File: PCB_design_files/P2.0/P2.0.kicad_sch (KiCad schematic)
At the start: 28 parts, among them J1 EEG+, J2 EEG-, U1 INA819IDRGR, U2 TLV9102

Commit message: More P2.0 schematic work
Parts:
- added BT1: BHSD-1225-SM, BHSD-1225-SM:BAT_BHSD-1225-SM, symbol Device:Battery_Cell
- added C10, C11: 10uF, Capacitor_SMD:C_0805_2012Metric, symbol Device:C
- added C8: 2.2uF, Capacitor_SMD:C_0402_1005Metric, symbol Device:C
- added C9: 33uF, Capacitor_SMD:C_0805_2012Metric, symbol Device:C
- added D1: LED, symbol Device:LED
- added L1: 2.2uH, symbol Device:L
- added R18, R19: 1.1k, Resistor_SMD:R_0402_1005Metric, symbol Device:R
- added U3: TPS61094, symbol My_Library:TPS61094
- added U4: TC1044S, symbol Regulator_SwitchedCapacitor:LTC1044
- added U5: NRF52832-QFAA-R, QFN-48_NOR, symbol NRF52832_QFAA:NRF52832-QFAA-R
- C1, C2, C7: footprint Library:CL10A106MQ8NNNC -> Capacitor_SMD:C_0805_2012Metric
- C3, C4, C5, C6: footprint Library:CL10A106MQ8NNNC -> Capacitor_SMD:C_0201_0603Metric
- R10, R11, R12, R13, R14, R2, R3, R4, R5, R6, R7, R8, R9: footprint (none) -> Resistor_SMD:R_0402_1005Metric
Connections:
- net +3V3: now also C9.2, U3.10 (VOUT), U4.8 (V+)
- net -3V3: now also C11.2, U4.5 (VOUT)
- net GND: now also BT1.2 (-), C11.1, C8.1, C9.1, D1.1 (K), R19.2, U3.11 (ICHG), U3.12 (VCHG), U3.7 (PGND), U3.8 (AGND), U4.3 (GND), U4.6 (LV)
- new net: C10.1, U4.4 (CAP-)
- new net: C10.2, U4.2 (CAP+)
- new net: BT1.1 (+), C8.2, L1.1, R18.1, U3.2 (MODE), U3.3 (EN), U3.4 (VIN), U3.6 (SUP)
- new net: L1.2, U3.5 (SW)
- new net: R19.1, U3.1 (OSEL)
- new net: D1.2 (A), R18.2
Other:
- note added: "2.Power Supply"
- note added: "3.Microcontroller"
- company: (none) -> JY-68
- title: (none) -> Wearable EEG Sensor
- moved on the sheet: C1, C2, C3, C4, C5, C6, C7, J1, J2, R1, R10, R11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

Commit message: Started PCB
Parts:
- L1: footprint (none) -> Inductor_SMD:L_Murata_DFE201610P
- R16, R17: footprint (none) -> Resistor_SMD:R_0402_1005Metric
- R18: footprint Resistor_SMD:R_0402_1005Metric -> (none)
- U5: footprint QFN-48_NOR -> (none)
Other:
- moved on the sheet: BT1, C10, C11, C8, C9, D1, L1, R18, R19, U3, U4, U5

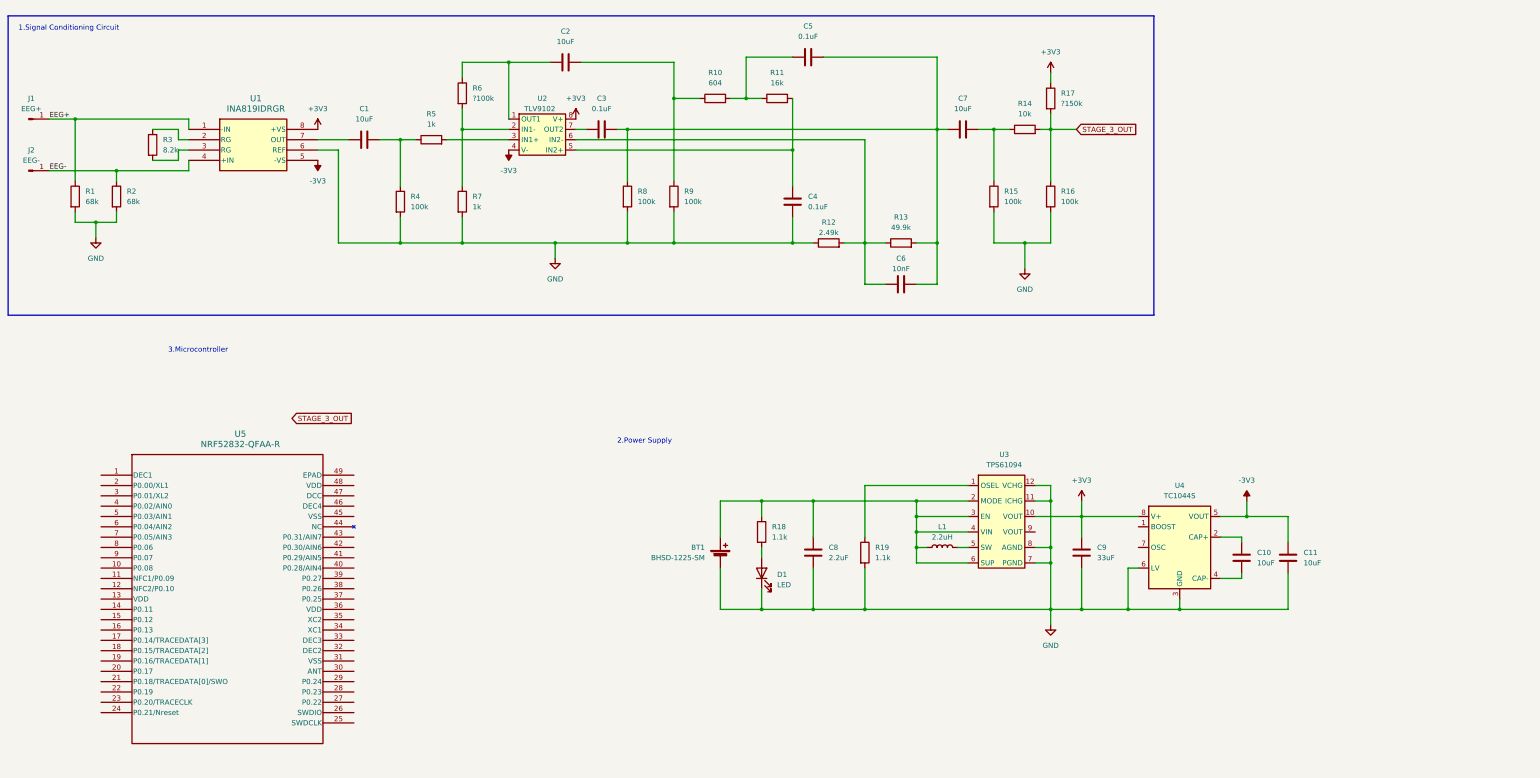
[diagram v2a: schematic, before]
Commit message: PCB layout and component footprint updates
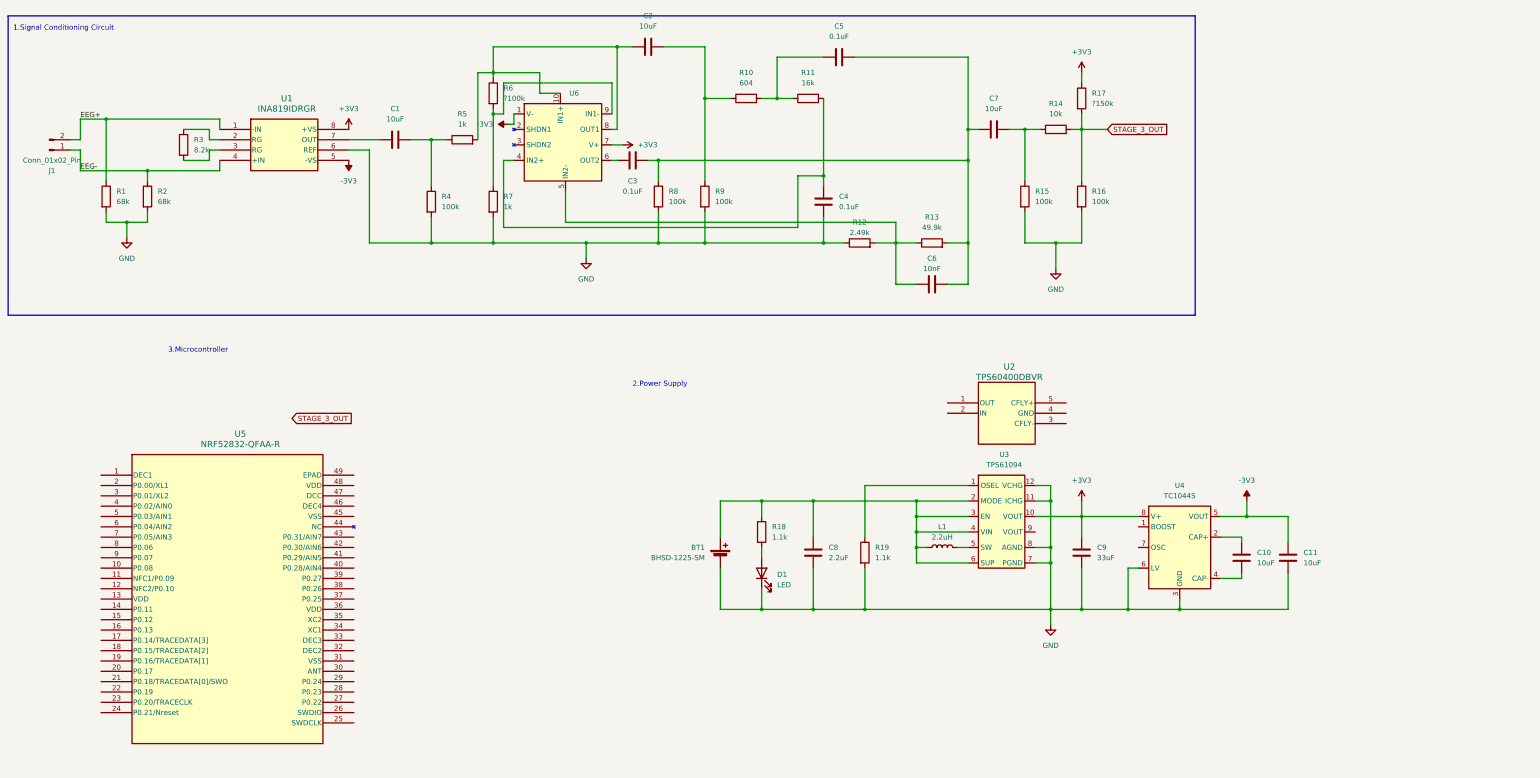
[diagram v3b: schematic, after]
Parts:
- removed J1: EEG+, symbol Connector:Conn_01x01_Pin
- removed J2: EEG-, symbol Connector:Conn_01x01_Pin
- removed U2: TLV9102, symbol My_Library:TLV9102
- added J1: Conn_01x02_Pin, Connector_JST:JST_SH_BM02B-SRSS-TB_1x02-1MP_P1.00mm_Vertical, symbol Connector:Conn_01x02_Pin
- added U2: TPS60400DBVR, DBV5, symbol TPS60400DBVR:TPS60400DBVR
- added U6: ~, symbol TLV9102SIRUGR:TLV9102
- BT1: footprint BHSD-1225-SM:BAT_BHSD-1225-SM -> Connector_JST:JST_ACH_BM02B-ACHSS-GAN-ETF_1x02-1MP_P1.20mm_Vertical
- D1: footprint (none) -> LED_SMD:LED_0402_1005Metric
- R15, R18: footprint (none) -> Resistor_SMD:R_0402_1005Metric
- U3: footprint (none) -> Library:TPS61094DSSR
- U4: footprint (none) -> Library:TC1044SEOA713
- U5: footprint (none) -> Library:QFN-48_NOR
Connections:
- net +3V3: now also U6.7 (V+)
- net -3V3: now also U6.1 (V-)
- net EEG+: now also J1.2 (Pin_2)
- net EEG-: now also J1.1 (Pin_1)
- net at C6.1, R12.2, R13.1: now also U6.5 (IN2-)
- net at C2.1, R6.1: now also R5.2, U6.10 (IN1+), U6.8 (OUT1)
- net at R6.2, R7.1: now also U6.9 (IN1-)
- net at C4.2, R11.2: now also U6.4 (IN2+)
- net at C3.1: now also U6.6 (OUT2)
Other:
- moved on the sheet: C1, C2, C3, C4, C5, C6, C7, R1, R10, R11, R12, R13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

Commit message: Done
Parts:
- removed U4: TC1044S, Library:TC1044SEOA713, symbol Regulator_SwitchedCapacitor:LTC1044
- C10, C11: value 10uF -> 1uF
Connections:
- net +3V3: now also U2.2 (IN)
- net -3V3: now also U2.1 (OUT)
- net GND: now also U2.4 (GND)
- net at C10.1: now also U2.5 (CFLY+)
- net at C10.2: now also U2.3 (CFLY-)
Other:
- moved on the sheet: C10, U2
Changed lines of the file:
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@@
   (junction (at 212.09 161.29) (diameter 0) (color 0 0 0 0)
   )
-  (junction (at 289.56 161.29) (diameter 0) (color 0 0 0 0)
-  )
   (junction (at 271.78 71.12) (diameter 0) (color 0 0 0 0)
   )
@@
     (stroke (width 0) (type default))
   )
+  (wire (pts (xy 299.72 140.97) (xy 298.45 140.97))
+    (stroke (width 0) (type default))
+  )
   (wire (pts (xy 278.13 161.29) (xy 270.51 161.29))
     (stroke (width 0) (type default))
@@
     (stroke (width 0) (type default))
   )
+  (wire (pts (xy 295.91 158.75) (xy 302.26 158.75))
+    (stroke (width 0) (type default))
+  )
   (wire (pts (xy 66.04 43.18) (xy 66.04 40.64))
     (stroke (width 0) (type default))
@@
     (stroke (width 0) (type default))
   )
+  (wire (pts (xy 298.45 140.97) (xy 298.45 151.13))
+    (stroke (width 0) (type default))
+  )
+  (wire (pts (xy 312.42 138.43) (xy 312.42 111.76))
+    (stroke (width 0) (type default))
+  )
   (wire (pts (xy 270.51 146.05) (xy 270.51 149.86))
     (stroke (width 0) (type default))
@@
     (stroke (width 0) (type default))
   )
+  (wire (pts (xy 306.07 151.13) (xy 306.07 140.97))
+    (stroke (width 0) (type default))
+  )
   (wire (pts (xy 199.39 156.21) (xy 199.39 161.29))
     (stroke (width 0) (type default))
@@
     (stroke (width 0) (type default))
   )
-  (wire (pts (xy 278.13 161.29) (xy 289.56 161.29))
+  (wire (pts (xy 278.13 161.29) (xy 302.26 161.29))
     (stroke (width 0) (type default))
   )
@@
     (stroke (width 0) (type default))
   )
-  (wire (pts (xy 289.56 151.13) (xy 289.56 161.29))
-    (stroke (width 0) (type default))
-  )
   (wire (pts (xy 57.15 50.8) (xy 63.5 50.8))
     (stroke (width 0) (type default))
@@
     (stroke (width 0) (type default))
   )
+  (wire (pts (xy 306.07 140.97) (xy 304.8 140.97))
+    (stroke (width 0) (type default))
+  )
   (wire (pts (xy 38.1 40.64) (xy 31.75 40.64))
     (stroke (width 0) (type default))
@@
     (stroke (width 0) (type default))
   )
+  (wire (pts (xy 302.26 140.97) (xy 302.26 146.05))
+    (stroke (width 0) (type default))
+  )
   (wire (pts (xy 266.7 130.81) (xy 270.51 130.81))
     (stroke (width 0) (type default))
@@
     (stroke (width 0) (type default))
   )
+  (wire (pts (xy 295.91 146.05) (xy 295.91 158.75))
+    (stroke (width 0) (type default))
+  )
   (wire (pts (xy 237.49 138.43) (xy 237.49 142.24))
     (stroke (width 0) (type default))
@@
     (stroke (width 0) (type default))
   )
-  (wire (pts (xy 317.5 143.51) (xy 312.42 143.51))
-    (stroke (width 0) (type default))
-  )
   (wire (pts (xy 151.13 66.04) (xy 232.41 66.04))
     (stroke (width 0) (type default))
@@
     (stroke (width 0) (type default))
   )
-  (wire (pts (xy 317.5 152.4) (xy 317.5 153.67))
-    (stroke (width 0) (type default))
-  )
   (wire (pts (xy 135.89 50.8) (xy 135.89 67.31))
     (stroke (width 0) (type default))
@@
     (stroke (width 0) (type default))
   )
-  (wire (pts (xy 289.56 151.13) (xy 292.1 151.13))
-    (stroke (width 0) (type default))
-  )
   (wire (pts (xy 171.45 50.8) (xy 173.99 50.8))
     (stroke (width 0) (type default))
@@
     (stroke (width 0) (type default))
   )
-  (wire (pts (xy 302.26 161.29) (xy 289.56 161.29))
-    (stroke (width 0) (type default))
-  )
   (wire (pts (xy 189.23 151.13) (xy 189.23 161.29))
     (stroke (width 0) (type default))
@@
     (stroke (width 0) (type default))
   )
+  (wire (pts (xy 302.26 111.76) (xy 292.1 111.76))
+    (stroke (width 0) (type default))
+  )
+  (wire (pts (xy 292.1 111.76) (xy 292.1 138.43))
+    (stroke (width 0) (type default))
+  )
   (wire (pts (xy 144.78 29.21) (xy 144.78 34.29))
     (stroke (width 0) (type default))
@@
     (stroke (width 0) (type default))
   )
+  (wire (pts (xy 302.26 146.05) (xy 295.91 146.05))
+    (stroke (width 0) (type default))
+  )
   (wire (pts (xy 38.1 40.64) (xy 66.04 40.64))
     (stroke (width 0) (type default))
   )
+  (wire (pts (xy 304.8 111.76) (xy 312.42 111.76))
+    (stroke (width 0) (type default))
+  )
   (wire (pts (xy 97.79 45.72) (xy 105.41 45.72))
     (stroke (width 0) (type default))
@@
     (stroke (width 0) (type default))
   )
-  (wire (pts (xy 317.5 144.78) (xy 317.5 143.51))
-    (stroke (width 0) (type default))
-  )
   (wire (pts (xy 133.35 71.12) (xy 133.35 64.77))
     (stroke (width 0) (type default))
@@
   )
   (wire (pts (xy 318.77 134.62) (xy 318.77 138.43))
-    (stroke (width 0) (type default))
-  )
-  (wire (pts (xy 317.5 153.67) (xy 312.42 153.67))
     (stroke (width 0) (type default))
   )
@@
     )
   )
-  (symbol (lib_id "Device:C") (at 317.5 148.59 180) (unit 1)
-    (in_bom yes) (on_board yes) (dnp no) (fields_autoplaced)
-    (property "Reference" "C10" (at 321.31 147.32 0)
-      (effects (font (size 1.27 1.27)) (justify right))
-    )
-    (property "Value" "10uF" (at 321.31 149.86 0)
-      (effects (font (size 1.27 1.27)) (justify right))
-    )
-    (property "Footprint" "Capacitor_SMD:C_0805_2012Metric" (at 316.5348 144.78 0)
-      (effects (font (size 1.27 1.27)) hide)
-    )
-    (property "Datasheet" "~" (at 317.5 148.59 0)
+  (symbol (lib_id "Device:C") (at 302.26 151.13 270) (unit 1)
+    (in_bom yes) (on_board yes) (dnp no) (fields_autoplaced)
+    (property "Reference" "C10" (at 302.26 143.51 90)
+      (effects (font (size 1.27 1.27)))
+    )
+    (property "Value" "1uF" (at 302.26 146.05 90)
+      (effects (font (size 1.27 1.27)))
+    )
+    (property "Footprint" "Capacitor_SMD:C_0805_2012Metric" (at 298.45 152.0952 0)
+      (effects (font (size 1.27 1.27)) hide)
+    )
+    (property "Datasheet" "~" (at 302.26 151.13 0)
       (effects (font (size 1.27 1.27)) hide)
     )
@@
     )
   )
-  (symbol (lib_id "Regulator_SwitchedCapacitor:LTC1044") (at 302.26 146.05 0) (unit 1)
-    (in_bom yes) (on_board yes) (dnp no) (fields_autoplaced)
-    (property "Reference" "U4" (at 302.26 130.81 0)
-      (effects (font (size 1.27 1.27)))
-    )
-    (property "Value" "TC1044S" (at 302.26 133.35 0)
-      (effects (font (size 1.27 1.27)))
-    )
-    (property "Footprint" "Library:TC1044SEOA713" (at 304.8 148.59 0)
-      (effects (font (size 1.27 1.27)) hide)
-    )
-    (property "Datasheet" "" (at 304.8 148.59 0)
-      (effects (font (size 1.27 1.27)) hide)
-    )
-    (pin "1")
-    (pin "7")
-    (pin "2")
-    (pin "5")
-    (pin "4")
-    (pin "6")
-    (pin "3")
-    (pin "8")
-    (instances
-      (project "P2.0"
-        (path "/cc4d5c34-4776-48f9-a8ce-15f2c8e358ac"
-          (reference "U4") (unit 1)
-        )
-      )
-    )
-  )
   (symbol (lib_id "Device:R") (at 133.35 34.29 0) (unit 1)
     (in_bom yes) (on_board yes) (dnp no) (fields_autoplaced)
@@
       (effects (font (size 1.27 1.27)) (justify right))
     )
-    (property "Value" "10uF" (at 332.74 149.86 0)
+    (property "Value" "1uF" (at 332.74 149.86 0)
       (effects (font (size 1.27 1.27)) (justify right))
     )
@@
     )
   )
-  (symbol (lib_id "TPS60400DBVR:TPS60400DBVR") (at 252.73 105.41 0) (unit 1)
+  (symbol (lib_id "TPS60400DBVR:TPS60400DBVR") (at 309.88 119.38 270) (unit 1)
     (in_bom yes) (on_board yes) (dnp no)
-    (property "Reference" "U2" (at 260.35 101.6 0)
+    (property "Reference" "U2" (at 313.69 127 0)
       (effects (font (size 1.524 1.524)))
     )
-    (property "Value" "TPS60400DBVR" (at 260.35 104.14 0)
+    (property "Value" "TPS60400DBVR" (at 311.15 127 0)
       (effects (font (size 1.524 1.524)))
     )
-    (property "Footprint" "DBV5" (at 252.73 105.41 0)
+    (property "Footprint" "DBV5" (at 309.88 119.38 0)
       (effects (font (size 1.27 1.27) italic) hide)
     )
-    (property "Datasheet" "TPS60400DBVR" (at 252.73 105.41 0)
+    (property "Datasheet" "TPS60400DBVR" (at 309.88 119.38 0)
       (effects (font (size 1.27 1.27) italic) hide)
     )

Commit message: Increased board size
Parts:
- U2: value TPS60400DBVR -> ~; footprint DBV5 -> (none)
- renumbered U6 to U2
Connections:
- net +3V3: no longer U2.2 (IN)
- net -3V3: no longer U2.1 (OUT)
- net GND: no longer U2.4 (GND)
- net at C10.1: no longer U2.5 (CFLY+)
- net at C10.2: now also U2.7 (V+); no longer U2.3 (CFLY-)
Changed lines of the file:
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@@
   (symbol (lib_id "TLV9102SIRUGR:TLV9102") (at 140.97 36.83 0) (unit 1)
     (in_bom yes) (on_board yes) (dnp no) (fields_autoplaced)
-    (property "Reference" "U6" (at 152.0541 34.29 0)
+    (property "Reference" "U2" (at 152.4 33.02 0)
       (effects (font (size 1.27 1.27)) (justify left))
     )
@@
       (project "P2.0"
         (path "/cc4d5c34-4776-48f9-a8ce-15f2c8e358ac"
-          (reference "U6") (unit 1)
+          (reference "U2") (unit 1)
         )
       )
@@
   (symbol (lib_id "TPS60400DBVR:TPS60400DBVR") (at 309.88 119.38 270) (unit 1)
     (in_bom yes) (on_board yes) (dnp no)
-    (property "Reference" "U2" (at 313.69 127 0)
-      (effects (font (size 1.524 1.524)))
+    (property "Reference" "U2" (at 313.69 130.81 0)
+      (effects (font (size 1.27 1.27)) (justify left))
     )
-    (property "Value" "TPS60400DBVR" (at 311.15 127 0)
-      (effects (font (size 1.524 1.524)))
+    (property "Value" "~" (at 309.88 119.38 0)
+      (effects (font (size 1.27 1.27)))
     )
-    (property "Footprint" "DBV5" (at 309.88 119.38 0)
-      (effects (font (size 1.27 1.27) italic) hide)
+    (property "Footprint" "" (at 309.88 119.38 0)
+      (effects (font (size 1.27 1.27)) hide)
     )
-    (property "Datasheet" "TPS60400DBVR" (at 309.88 119.38 0)
-      (effects (font (size 1.27 1.27) italic) hide)
+    (property "Datasheet" "" (at 309.88 119.38 0)
+      (effects (font (size 1.27 1.27)) hide)
     )
     (pin "3")
@@
     (pin "2")
     (pin "1")
+    (pin "8")
+    (pin "6")
+    (pin "7")
+    (pin "9")
+    (pin "10")
     (instances
       (project "P2.0"

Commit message: Updated P2.0
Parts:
- added AE1: Antenna_Chip, Library:XDCR_2450AT18B100E, symbol Device:Antenna_Chip
- added C12, C13, C14: 100nF, Capacitor_SMD:C_0402_1005Metric, symbol Device:C
- added C15: 1.2pF, Capacitor_SMD:C_0402_1005Metric, symbol Device:C
- added C16, C18: 12pF, Capacitor_SMD:C_0402_1005Metric, symbol Device:C
- added C17: 100pF, Capacitor_SMD:C_0402_1005Metric, symbol Device:C
- added C19: 1uF, Capacitor_SMD:C_0603_1608Metric, symbol Device:C
- added C20: 4.7uF, Capacitor_SMD:C_0603_1608Metric, symbol Device:C
- added C21: N.C., Capacitor_SMD:C_0402_1005Metric, symbol Device:C
- added J3: SWD, symbol Connector:Conn_01x03_Pin
- added L2: 3.3nH, Inductor_SMD:L_0402_1005Metric, symbol Device:L
- added L3: 2.7nH, Inductor_SMD:L_0402_1005Metric, symbol Device:L
- added R20: 10k, Resistor_SMD:R_0402_1005Metric, symbol Device:R
- added X1: 32MHz, symbol Device:Crystal
- J1: value Conn_01x02_Pin -> EEG_IN
- renumbered U2 to U4
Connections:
- net +3V3: now also U5.13 (VDD), U5.36 (VDD), U5.48 (VDD), C13.2, C14.1, C20.1
- net -3V3: now also U4.10 (IN1+)
- net GND: now also U5.31 (VSS), U5.45 (VSS), C12.2, C13.1, C14.2, C16.1, C17.1, C18.1, C19.2, C20.2, C21.1, J3.1 (Pin_1), L3.1
- net STAGE_3_OUT: now also R20.1
- net at U5.1 (DEC1): now also C12.1
- net at U5.25 (SWDCLK): now also J3.2 (Pin_2)
- net at U5.26 (SWDIO): now also J3.3 (Pin_3)
- net at U5.30 (ANT): now also C15.2
- net at U5.32 (DEC2): now also C21.2
- net at U5.33 (DEC3): now also C17.2
- net at U5.34 (XC1): now also C18.2, X1.1
- net at U5.35 (XC2): now also C16.2, X1.2
- net at U5.4 (P0.02/AIN0): now also R20.2
- net at U5.46 (DEC4): now also C19.1
- new net: C15.1, L2.1, L3.2
- new net: AE1.1 (FEED), L2.2
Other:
- note added: "2.Microcontroller"
- note added: "3.Power Supply"
- note removed: "2.Power Supply"
- note removed: "3.Microcontroller"
- moved on the sheet: BT1, C10, C11, C8, C9, D1, L1, R18, R19, U3, U4, U5

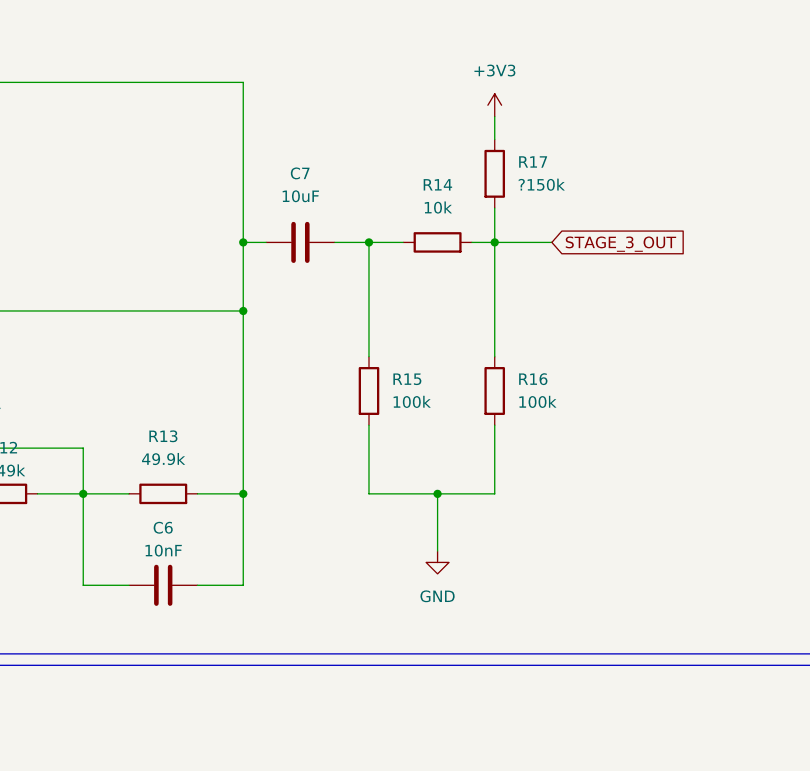
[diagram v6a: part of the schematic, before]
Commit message: Fixed  for P2.0
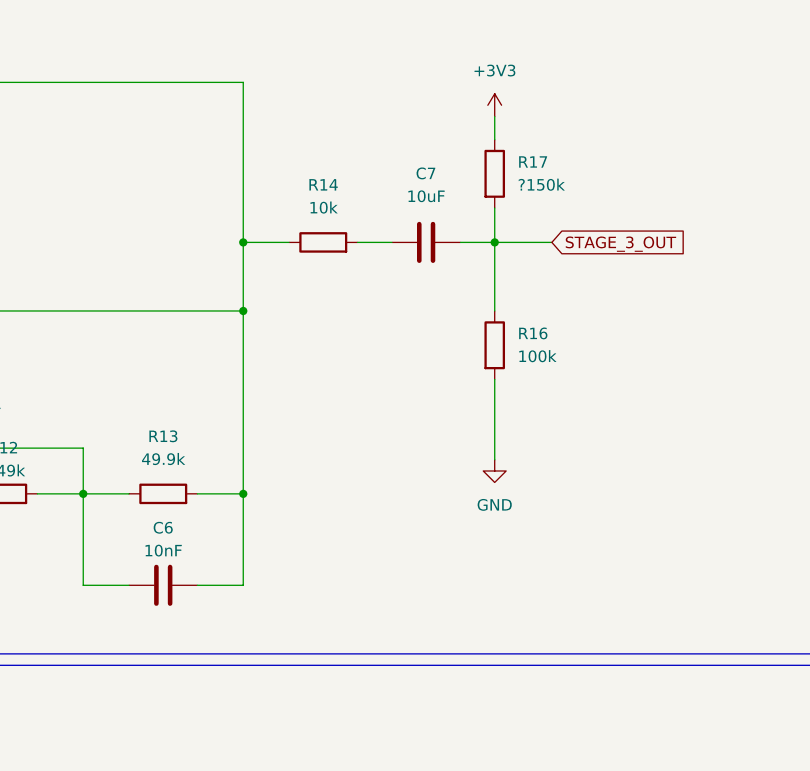
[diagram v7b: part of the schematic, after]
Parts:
- removed R15: 100k, Resistor_SMD:R_0402_1005Metric, symbol Device:R
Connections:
- net STAGE_3_OUT: now also C7.2; no longer R14.2
- net at C3.2, C5.1, C6.2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: now also R14.1; no longer C7.1
- new net: C7.1, R14.2
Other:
- moved on the sheet: C7, R14, R16
